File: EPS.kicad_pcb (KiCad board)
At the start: 4 copper layers, 90.2 x 95.9 mm, 6 parts

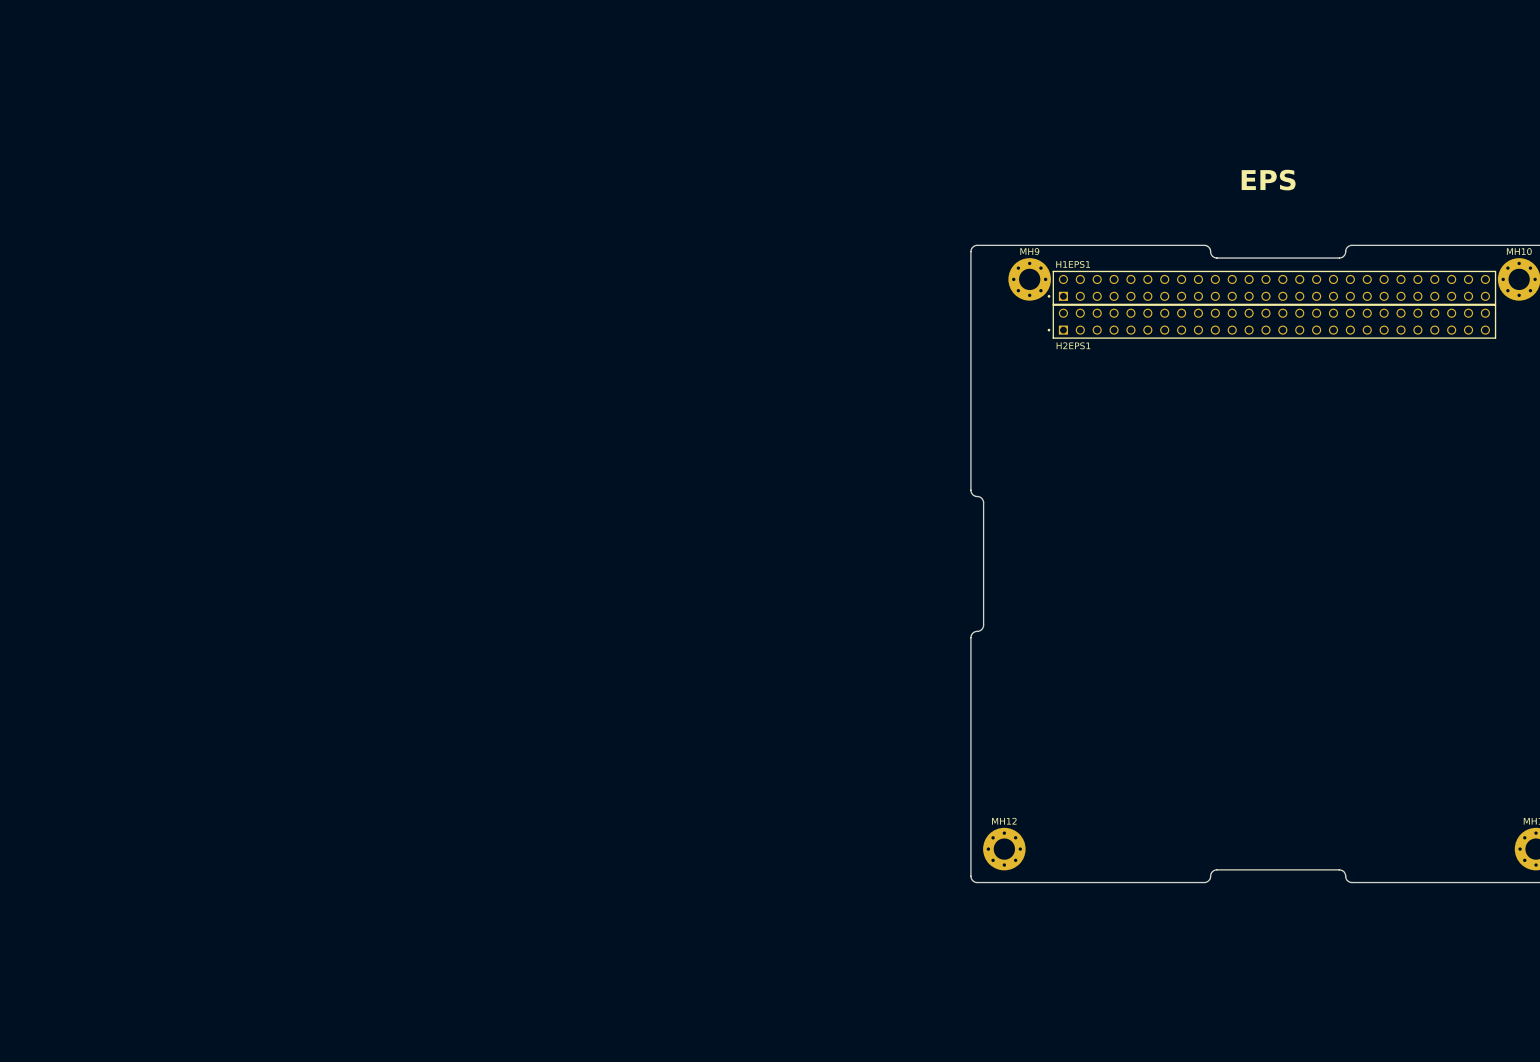
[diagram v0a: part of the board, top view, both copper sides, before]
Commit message: updated the schematic to remove connection to rocksat, linked schmatic symbols to footprints
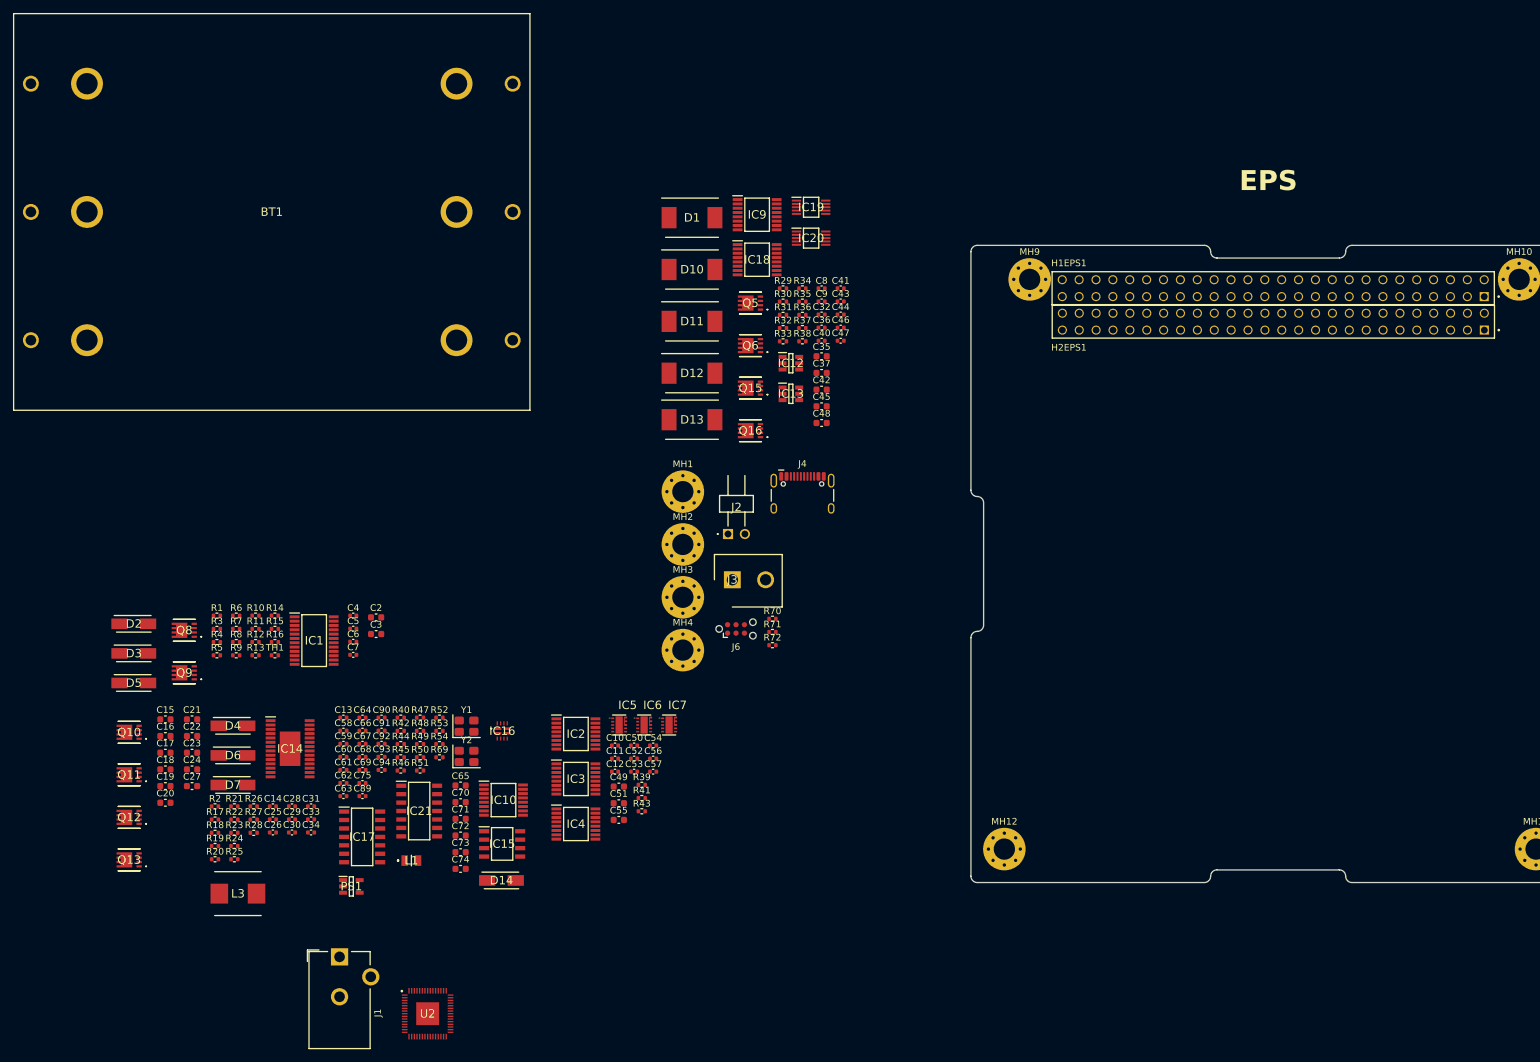
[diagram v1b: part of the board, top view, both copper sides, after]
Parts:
- added BT1: BK-18650-PC6, HEDGE2:BK18650PC6, F.Cu at (71.2, 86.3)
- added C10: 100n, Capacitor_SMD:C_0402_1005Metric, F.Cu at (122.8, 166.6)
- added C11: 100n, Capacitor_SMD:C_0402_1005Metric, F.Cu at (122.8, 168.6)
- added C12: 100n, Capacitor_SMD:C_0402_1005Metric, F.Cu at (122.8, 170.5)
- added C13: 100n, Capacitor_SMD:C_0402_1005Metric, F.Cu at (81.9, 162.4)
- added C14: 100n, Capacitor_SMD:C_0402_1005Metric, F.Cu at (71.3, 175.7)
- added C15: 33u, Capacitor_SMD:C_0603_1608Metric, F.Cu at (55.1, 162.7)
- added C16: 33u, Capacitor_SMD:C_0603_1608Metric, F.Cu at (55.1, 165.2)
- added C17: 33u, Capacitor_SMD:C_0603_1608Metric, F.Cu at (55.1, 167.7)
- added C18: 10u, Capacitor_SMD:C_0603_1608Metric, F.Cu at (55.1, 170.2)
- added C19: 10u, Capacitor_SMD:C_0603_1608Metric, F.Cu at (55.1, 172.7)
- added C2: 1u, Capacitor_SMD:C_0603_1608Metric, F.Cu at (86.8, 147.3)
- added C20: 22u, Capacitor_SMD:C_0603_1608Metric, F.Cu at (55.1, 175.2)
- added C21: 22u, Capacitor_SMD:C_0603_1608Metric, F.Cu at (59.1, 162.7)
- added C22: 22u, Capacitor_SMD:C_0603_1608Metric, F.Cu at (59.1, 165.2)
- added C23: 220u, Capacitor_SMD:C_0603_1608Metric, F.Cu at (59.1, 167.7)
- added C24: 220u, Capacitor_SMD:C_0603_1608Metric, F.Cu at (59.1, 170.2)
- added C25: 100n, Capacitor_SMD:C_0402_1005Metric, F.Cu at (71.3, 177.7)
- added C26: 100n, Capacitor_SMD:C_0402_1005Metric, F.Cu at (71.3, 179.7)
- added C27: 1u, Capacitor_SMD:C_0603_1608Metric, F.Cu at (59.1, 172.7)
- added C28: 100n, Capacitor_SMD:C_0402_1005Metric, F.Cu at (74.2, 175.7)
- added C29: 47p, Capacitor_SMD:C_0402_1005Metric, F.Cu at (74.2, 177.7)
- added C3: 1u, Capacitor_SMD:C_0603_1608Metric, F.Cu at (86.8, 149.8)
- added C30: 15n, Capacitor_SMD:C_0402_1005Metric, F.Cu at (74.2, 179.7)
- added C31: 15n, Capacitor_SMD:C_0402_1005Metric, F.Cu at (77.1, 175.7)
- added C32: 22n, Capacitor_SMD:C_0402_1005Metric, F.Cu at (153.9, 101.7)
- added C33: 180p, Capacitor_SMD:C_0402_1005Metric, F.Cu at (77.1, 177.7)
- added C34: 100p, Capacitor_SMD:C_0402_1005Metric, F.Cu at (77.1, 179.7)
- added C35: 47u, Capacitor_SMD:C_0603_1608Metric, F.Cu at (153.9, 108.0)
- added C36: 100n, Capacitor_SMD:C_0402_1005Metric, F.Cu at (153.9, 103.7)
- added C37: 22u, Capacitor_SMD:C_0603_1608Metric, F.Cu at (153.9, 110.5)
- added C4: 100n, Capacitor_SMD:C_0402_1005Metric, F.Cu at (83.4, 147.0)
- added C40: 22n, Capacitor_SMD:C_0402_1005Metric, F.Cu at (153.9, 105.7)
- added C41: 100n, Capacitor_SMD:C_0402_1005Metric, F.Cu at (156.8, 97.8)
- added C42: 22u, Capacitor_SMD:C_0603_1608Metric, F.Cu at (153.9, 113.0)
- added C43: 100n, Capacitor_SMD:C_0402_1005Metric, F.Cu at (156.8, 99.8)
- added C44: 100n, Capacitor_SMD:C_0402_1005Metric, F.Cu at (156.8, 101.7)
- added C45: 22u, Capacitor_SMD:C_0603_1608Metric, F.Cu at (153.9, 115.5)
- added C46: 100n, Capacitor_SMD:C_0402_1005Metric, F.Cu at (156.8, 103.7)
- added C47: 100n, Capacitor_SMD:C_0402_1005Metric, F.Cu at (156.8, 105.7)
- added C48: 22u, Capacitor_SMD:C_0603_1608Metric, F.Cu at (153.9, 118.1)
- added C49: 1u, Capacitor_SMD:C_0603_1608Metric, F.Cu at (123.4, 172.8)
- added C5: 100n, Capacitor_SMD:C_0402_1005Metric, F.Cu at (83.4, 149.0)
- added C50: 100n, Capacitor_SMD:C_0402_1005Metric, F.Cu at (125.7, 166.6)
- added C51: 1u, Capacitor_SMD:C_0603_1608Metric, F.Cu at (123.4, 175.3)
- added C52: 220p, Capacitor_SMD:C_0402_1005Metric, F.Cu at (125.7, 168.6)
- added C53: 220p, Capacitor_SMD:C_0402_1005Metric, F.Cu at (125.7, 170.5)
- added C54: 100n, Capacitor_SMD:C_0402_1005Metric, F.Cu at (128.5, 166.6)
- added C55: 1u, Capacitor_SMD:C_0603_1608Metric, F.Cu at (123.4, 177.8)
- added C56: 220p, Capacitor_SMD:C_0402_1005Metric, F.Cu at (128.5, 168.6)
- added C57: 100n, Capacitor_SMD:C_0402_1005Metric, F.Cu at (128.5, 170.5)
- added C58: 100n, Capacitor_SMD:C_0402_1005Metric, F.Cu at (81.9, 164.4)
- added C59: 100n, Capacitor_SMD:C_0402_1005Metric, F.Cu at (81.9, 166.3)
- added C6: 100n, Capacitor_SMD:C_0402_1005Metric, F.Cu at (83.4, 151.0)
- added C60: 100n, Capacitor_SMD:C_0402_1005Metric, F.Cu at (81.9, 168.3)
- added C61: 100n, Capacitor_SMD:C_0402_1005Metric, F.Cu at (81.9, 170.3)
- added C62: 100n, Capacitor_SMD:C_0402_1005Metric, F.Cu at (81.9, 172.2)
- added C63: 100n, Capacitor_SMD:C_0402_1005Metric, F.Cu at (81.9, 174.2)
- added C64: 100n, Capacitor_SMD:C_0402_1005Metric, F.Cu at (84.8, 162.4)
- added C65: 4u7, Capacitor_SMD:C_0603_1608Metric, F.Cu at (99.6, 172.6)
- added C66: 100n, Capacitor_SMD:C_0402_1005Metric, F.Cu at (84.8, 164.4)
- added C67: 100n, Capacitor_SMD:C_0402_1005Metric, F.Cu at (84.8, 166.3)
- added C68: 15p, Capacitor_SMD:C_0402_1005Metric, F.Cu at (84.8, 168.3)
- added C69: 15p, Capacitor_SMD:C_0402_1005Metric, F.Cu at (84.8, 170.3)
- added C7: 100n, Capacitor_SMD:C_0402_1005Metric, F.Cu at (83.4, 152.9)
- added C70: 4u7, Capacitor_SMD:C_0603_1608Metric, F.Cu at (99.6, 175.1)
- added C71: 4u7, Capacitor_SMD:C_0603_1608Metric, F.Cu at (99.6, 177.6)
- added C72: 4u7, Capacitor_SMD:C_0603_1608Metric, F.Cu at (99.6, 180.1)
- added C73: 1u, Capacitor_SMD:C_0603_1608Metric, F.Cu at (99.6, 182.7)
- added C74: 1u, Capacitor_SMD:C_0603_1608Metric, F.Cu at (99.6, 185.2)
- added C75: 100n, Capacitor_SMD:C_0402_1005Metric, F.Cu at (84.8, 172.2)
- added C8: 100n, Capacitor_SMD:C_0402_1005Metric, F.Cu at (153.9, 97.8)
- added C89: 100n, Capacitor_SMD:C_0402_1005Metric, F.Cu at (84.8, 174.2)
- added C9: 100n, Capacitor_SMD:C_0402_1005Metric, F.Cu at (153.9, 99.8)
- added C90: 100n, Capacitor_SMD:C_0402_1005Metric, F.Cu at (87.7, 162.4)
- added C91: 100n, Capacitor_SMD:C_0402_1005Metric, F.Cu at (87.7, 164.4)
- added C92: 100n, Capacitor_SMD:C_0402_1005Metric, F.Cu at (87.7, 166.3)
- added C93: 15p, Capacitor_SMD:C_0402_1005Metric, F.Cu at (87.7, 168.3)
- added C94: 15p, Capacitor_SMD:C_0402_1005Metric, F.Cu at (87.7, 170.3)
- added D1: SMCJ36A, HEDGE2:SMCJ36A, F.Cu at (134.4, 87.2)
- added D10: SMCJ36A, HEDGE2:SMCJ36A, F.Cu at (134.4, 95.0)
- added D11: SMCJ36A, HEDGE2:SMCJ36A, F.Cu at (134.4, 102.8)
- added D12: SMCJ36A, HEDGE2:SMCJ36A, F.Cu at (134.4, 110.6)
- added D13: SMCJ36A, HEDGE2:SMCJ36A, F.Cu at (134.4, 117.6)
- added D14: CDBA240LL-HF, 40V 2A, HEDGE2:CDBA240LL-HF, F.Cu at (105.7, 186.9)
- added D2: CDBA240LL-HF, 40V 2A, HEDGE2:CDBA240LL-HF, F.Cu at (50.4, 148.3)
- added D3: CDBA240LL-HF, 40V 2A, HEDGE2:CDBA240LL-HF, F.Cu at (50.4, 152.7)
- added D4: 40V 2A, HEDGE2:CDBA240LL-HF, F.Cu at (65.3, 163.6)
- added D5: CDBA240LL-HF, 40V 2A, HEDGE2:CDBA240LL-HF, F.Cu at (50.4, 157.2)
- added D6: CDBA240LL-HF, 40V 2A, HEDGE2:CDBA240LL-HF, F.Cu at (65.3, 168.1)
- added D7: 40V 2A, HEDGE2:CDBA240LL-HF, F.Cu at (65.3, 172.5)
- added IC1: BQ7791514PWR, HEDGE2:BQ7791501PWR, F.Cu at (77.5, 150.8)
- added IC10: INA260AIPWR, HEDGE2:INA260AIPWR, F.Cu at (106.0, 174.8)
- added IC12: LM74700QDBVRQ1, HEDGE2:LM74700QDBVRQ1, F.Cu at (149.3, 109.1)
- added IC13: LM74700QDBVRQ1, HEDGE2:LM74700QDBVRQ1, F.Cu at (149.3, 113.7)
- added IC14: LM5176PWPR, HEDGE2:LM5176PWPR, F.Cu at (73.9, 167.1)
- added IC15: SN65HVD1782QDRQ1, HEDGE2:SN65HVD1782QDRQ1, F.Cu at (105.8, 181.4)
- added IC16: TPS2121RUXR, HEDGE2:TPS2121RUXR, F.Cu at (105.8, 164.4)
- added IC17: TCAN1046AVDRQ1, HEDGE2:TCAN1046AVDRQ1, F.Cu at (84.7, 180.3)
- added IC18: INA260AIPWR, HEDGE2:INA260AIPWR, F.Cu at (144.2, 93.5)
- added IC19: LM5060Q1MM_NOPB, HEDGE2:LM5060Q1MM_NOPB, F.Cu at (152.3, 85.6)
- added IC2: INA260AIPWR, HEDGE2:INA260AIPWR, F.Cu at (116.9, 164.9)
- added IC20: LM5060Q1MM_NOPB, HEDGE2:LM5060Q1MM_NOPB, F.Cu at (152.3, 90.2)
- added IC21: MCP2517FD-H_SL, HEDGE2:MCP2517FD-H_SL, F.Cu at (93.3, 176.5)
- added IC3: INA260AIPWR, HEDGE2:INA260AIPWR, F.Cu at (116.9, 171.6)
- added IC4: INA260AIPWR, HEDGE2:INA260AIPWR, F.Cu at (116.9, 178.4)
- added IC5: TPS22990DMLR, HEDGE2:TPS22990DMLR, F.Cu at (123.4, 163.5)
- added IC6: TPS22990DMLR, HEDGE2:TPS22990DMLR, F.Cu at (127.2, 163.5)
- added IC7: TPS22990DMLR, HEDGE2:TPS22990DMLR, F.Cu at (130.9, 163.5)
- added IC9: INA260AIPWR, HEDGE2:INA260AIPWR, F.Cu at (144.2, 86.7)
- added J1: Barrel_Jack_Switch, Connector_BarrelJack:BarrelJack_CUI_PJ-102AH_Horizontal, F.Cu at (81.3, 198.4)
- added J2: PH1RA-02-UA, HEDGE2:PH1RA02UA, F.Cu at (139.8, 134.8)
- added J3: WJ126V-5.0-2P, HEDGE2:WJ126V-5.0-2P, F.Cu at (140.5, 141.7)
- added J4: USB_C_Receptacle_USB2.0_16P, Connector_USB:USB_C_Receptacle_HCTL_HC-TYPE-C-16P-01A, F.Cu at (151.0, 129.8)
- added J6: TagConnect_TC2030-NL, Connector:Tag-Connect_TC2030-IDC-NL_2x03_P1.27mm_Vertical, F.Cu at (141.0, 149.1)
- added L1: 3u3 AOTA-B201610S3R3-101-T, HEDGE2:AOTAB201610S3R3101T, F.Cu at (92.2, 183.9)
- added L3: 0630CDMCDDS-1R2MC, HEDGE2:0630CDMCDDS-1R2MC, F.Cu at (66.1, 188.9)
- added MH1: MountingHole_Pad, MountingHole:MountingHole_3.2mm_M3_Pad_Via, F.Cu at (133.0, 128.4)
- added MH2: MountingHole_Pad, MountingHole:MountingHole_3.2mm_M3_Pad_Via, F.Cu at (133.0, 136.3)
- added MH3: MountingHole_Pad, MountingHole:MountingHole_3.2mm_M3_Pad_Via, F.Cu at (133.0, 144.3)
- added MH4: MountingHole_Pad, MountingHole:MountingHole_3.2mm_M3_Pad_Via, F.Cu at (133.0, 152.2)
- added PS1: TLV75733PDBVR, HEDGE2:TLV75733PDBVR, F.Cu at (83.1, 187.8)
- added Q10: BSZ067N06LS3_G, HEDGE2:BSZ067N06LS3G, F.Cu at (49.7, 164.6)
- added Q11: BSZ067N06LS3_G, HEDGE2:BSZ067N06LS3G, F.Cu at (49.7, 171.0)
- added Q12: BSZ067N06LS3_G, HEDGE2:BSZ067N06LS3G, F.Cu at (49.7, 177.4)
- added Q13: BSZ067N06LS3_G, HEDGE2:BSZ067N06LS3G, F.Cu at (49.7, 183.8)
- added Q15: BSZ067N06LS3_G, HEDGE2:BSZ067N06LS3G, F.Cu at (143.2, 112.8)
- added Q16: BSZ067N06LS3_G, HEDGE2:BSZ067N06LS3G, F.Cu at (143.2, 119.2)
- added Q5: BSZ067N06LS3_G, HEDGE2:BSZ067N06LS3G, F.Cu at (143.2, 100.0)
- added Q6: BSZ067N06LS3_G, HEDGE2:BSZ067N06LS3G, F.Cu at (143.2, 106.4)
- added Q8: BSZ067N06LS3_G, HEDGE2:BSZ067N06LS3G, F.Cu at (58.0, 149.3)
- added Q9: BSZ067N06LS3_G, HEDGE2:BSZ067N06LS3G, F.Cu at (58.0, 155.7)
- added R1: 1k, Resistor_SMD:R_0402_1005Metric, F.Cu at (62.9, 147.1)
- added R10: 1M, Resistor_SMD:R_0402_1005Metric, F.Cu at (68.7, 147.1)
- added R11: 1M, Resistor_SMD:R_0402_1005Metric, F.Cu at (68.7, 149.0)
- added R12: 3M3, Resistor_SMD:R_0402_1005Metric, F.Cu at (68.7, 151.0)
- added R13: 450k, Resistor_SMD:R_0402_1005Metric, F.Cu at (68.7, 153.0)
- added R14: 100k, Resistor_SMD:R_0402_1005Metric, F.Cu at (71.6, 147.1)
- added R15: 10k, Resistor_SMD:R_0402_1005Metric, F.Cu at (71.6, 149.0)
- added R16: 10k, Resistor_SMD:R_0402_1005Metric, F.Cu at (71.6, 151.0)
- added R17: 10, Resistor_SMD:R_0402_1005Metric, F.Cu at (62.6, 177.7)
- added R18: 249k, Resistor_SMD:R_0402_1005Metric, F.Cu at (62.6, 179.7)
- added R19: 71k5, Resistor_SMD:R_0402_1005Metric, F.Cu at (62.6, 181.7)
- added R2: 9m, Resistor_SMD:R_0402_1005Metric, F.Cu at (62.6, 175.8)
- added R20: 2k, Resistor_SMD:R_0402_1005Metric, F.Cu at (62.6, 183.7)
- added R21: 105k, Resistor_SMD:R_0402_1005Metric, F.Cu at (65.5, 175.8)
- added R22: 20k, Resistor_SMD:R_0402_1005Metric, F.Cu at (65.5, 177.7)
- added R23: 10k, Resistor_SMD:R_0402_1005Metric, F.Cu at (65.5, 179.7)
- added R24: 100, Resistor_SMD:R_0402_1005Metric, F.Cu at (65.5, 181.7)
- added R25: 100, Resistor_SMD:R_0402_1005Metric, F.Cu at (65.5, 183.7)
- added R26: 93k1, Resistor_SMD:R_0402_1005Metric, F.Cu at (68.4, 175.8)
- added R27: 23k2, Resistor_SMD:R_0402_1005Metric, F.Cu at (68.4, 177.7)
- added R28: 7k5, Resistor_SMD:R_0402_1005Metric, F.Cu at (68.4, 179.7)
- added R29: 9k09, Resistor_SMD:R_0402_1005Metric, F.Cu at (148.1, 97.8)
- added R3: 1k, Resistor_SMD:R_0402_1005Metric, F.Cu at (62.9, 149.0)
- added R30: 100k, Resistor_SMD:R_0402_1005Metric, F.Cu at (148.1, 99.8)
- added R31: 200k, Resistor_SMD:R_0402_1005Metric, F.Cu at (148.1, 101.8)
- added R32: 38k3, Resistor_SMD:R_0402_1005Metric, F.Cu at (148.1, 103.8)
- added R33: 14k, Resistor_SMD:R_0402_1005Metric, F.Cu at (148.1, 105.8)
- added R34: 200k, Resistor_SMD:R_0402_1005Metric, F.Cu at (151.0, 97.8)
- added R35: 38k3, Resistor_SMD:R_0402_1005Metric, F.Cu at (151.0, 99.8)
- added R36: 14k, Resistor_SMD:R_0402_1005Metric, F.Cu at (151.0, 101.8)
- added R37: 9k09, Resistor_SMD:R_0402_1005Metric, F.Cu at (151.0, 103.8)
- added R38: 100k, Resistor_SMD:R_0402_1005Metric, F.Cu at (151.0, 105.8)
- added R39: 10k, Resistor_SMD:R_0402_1005Metric, F.Cu at (126.8, 172.5)
- added R4: 1k, Resistor_SMD:R_0402_1005Metric, F.Cu at (62.9, 151.0)
- added R40: 27, Resistor_SMD:R_0402_1005Metric, F.Cu at (90.6, 162.4)
- added R41: 10k, Resistor_SMD:R_0402_1005Metric, F.Cu at (126.8, 174.5)
- added R42: 27, Resistor_SMD:R_0402_1005Metric, F.Cu at (90.6, 164.4)
- added R43: 10k, Resistor_SMD:R_0402_1005Metric, F.Cu at (126.8, 176.5)
- added R44: 1k, Resistor_SMD:R_0402_1005Metric, F.Cu at (90.6, 166.4)
- added R45: 33, Resistor_SMD:R_0402_1005Metric, F.Cu at (90.6, 168.4)
- added R46: 23k7, Resistor_SMD:R_0402_1005Metric, F.Cu at (90.6, 170.4)
- added R47: 5k, Resistor_SMD:R_0402_1005Metric, F.Cu at (93.5, 162.4)
- added R48: 23k7, Resistor_SMD:R_0402_1005Metric, F.Cu at (93.5, 164.4)
- added R49: 5k, Resistor_SMD:R_0402_1005Metric, F.Cu at (93.5, 166.4)
- added R5: 1k, Resistor_SMD:R_0402_1005Metric, F.Cu at (62.9, 153.0)
- added R50: 51k1, Resistor_SMD:R_0402_1005Metric, F.Cu at (93.5, 168.4)
- added R51: 4k7, Resistor_SMD:R_0402_1005Metric, F.Cu at (93.5, 170.4)
- added R52: 4k7, Resistor_SMD:R_0402_1005Metric, F.Cu at (96.4, 162.4)
- added R53: 10k, Resistor_SMD:R_0402_1005Metric, F.Cu at (96.4, 164.4)
- added R54: 60, Resistor_SMD:R_0402_1005Metric, F.Cu at (96.4, 166.4)
- added R6: 1k, Resistor_SMD:R_0402_1005Metric, F.Cu at (65.8, 147.1)
- added R69: 60, Resistor_SMD:R_0402_1005Metric, F.Cu at (96.4, 168.4)
- added R7: 10m, Resistor_SMD:R_0402_1005Metric, F.Cu at (65.8, 149.0)
- added R70: 5k1, Resistor_SMD:R_0402_1005Metric, F.Cu at (146.5, 147.5)
- added R71: 5k1, Resistor_SMD:R_0402_1005Metric, F.Cu at (146.5, 149.5)
- added R72: 4k7, Resistor_SMD:R_0402_1005Metric, F.Cu at (146.5, 151.5)
- added R8: 4k5, Resistor_SMD:R_0402_1005Metric, F.Cu at (65.8, 151.0)
- added R9: 1M, Resistor_SMD:R_0402_1005Metric, F.Cu at (65.8, 153.0)
- added TH1: 10k, Resistor_SMD:R_0402_1005Metric, F.Cu at (71.6, 153.0)
- added U2: RP2354A_60QFN, HEDGE2:RP2354A, F.Cu at (94.6, 206.9)
- added Y1: ABM8AIG-20MHz-12-2Z-T3, Crystal:Crystal_SMD_3225-4Pin_3.2x2.5mm, F.Cu at (100.5, 163.7)
- added Y2: ABM8-272-T3, Crystal:Crystal_SMD_3225-4Pin_3.2x2.5mm, F.Cu at (100.5, 168.2)
- H1EPS1, H2EPS1: footprint ESQ-126-39-G-D:SAMTEC_ESQ-126-39-G-D -> HEDGE2:SAMTEC_ESQ-126-39-G-D
- moved H2EPS1 63.3 mm to (253.6, 104.1)
- moved H1EPS1 63.3 mm to (253.6, 99.0)
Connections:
- net /EPS/5V_PERM renamed /5V_PERM
- net /EPS/BATT renamed /BATT
- net /EPS/CAN_A_H renamed /CAN_A_H
- net /EPS/CAN_A_L renamed /CAN_A_L
- net /EPS/CAN_B_H renamed /CAN_B_H
- net /EPS/CAN_B_L renamed /CAN_B_L
- net /EPS/CHARGE renamed /CHARGE
- net /EPS/DS_A renamed /DS_A
- net /EPS/DS_B renamed /DS_B
- net /EPS/DS_C renamed /DS_C
- net /EPS/ENA_PWR_1 renamed /ENA_PWR_1
- net /EPS/ENA_PWR_2 renamed /ENA_PWR_2
- net /EPS/ENA_PWR_3 renamed /ENA_PWR_3
- net /EPS/ENA_PWR_4 renamed /ENA_PWR_4
- net /EPS/ENA_PWR_5 renamed /ENA_PWR_5
- net /EPS/ENA_PWR_6 renamed /ENA_PWR_6
- net /EPS/ENA_PWR_7 renamed /ENA_PWR_7
- net /EPS/ENA_PWR_8 renamed /ENA_PWR_8
- net /EPS/PWR_1 renamed /PWR_1
- net /EPS/PWR_2 renamed /PWR_2
- net /EPS/PWR_3 renamed /PWR_3
- net /EPS/PWR_4 renamed /PWR_4
- net /EPS/PWR_5 renamed /PWR_5
- net /EPS/PWR_6 renamed /PWR_6
- net /EPS/PWR_7 renamed /PWR_7
- net /EPS/PWR_8 renamed /PWR_8
- net /EPS/RBF_A renamed /RBF_A
- net /EPS/RBF_B renamed /RBF_B
- net /EPS/RBF_C renamed /RBF_C
- net /EPS/UART_A_RX renamed /UART_A_RX
- net /EPS/UART_A_TX renamed /UART_A_TX
- net /EPS/UART_B_RX renamed /UART_B_RX
- net /EPS/UART_B_TX renamed /UART_B_TX
- net /EPS/UART_C_RX renamed /UART_C_RX
- net /EPS/UART_C_TX renamed /UART_C_TX
- net /EPS/UART_D_RX renamed /UART_D_RX
- net /EPS/UART_D_TX renamed /UART_D_TX
- net /EPS/UART_E_RX renamed /UART_E_RX
- net /EPS/UART_E_TX renamed /UART_E_TX
- net /EPS/UART_F_RX renamed /UART_F_RX
- net /EPS/UART_F_TX renamed /UART_F_TX
- H1EPS1 pad 29: GND -> +BATT
- H1EPS1 pad 30: GND -> +BATT
- H1EPS1 pad 31: GND -> +BATT
- H1EPS1 pad 32: GND -> +BATT
- H2EPS1 pad 29: GND -> +BATT
- H2EPS1 pad 30: GND -> +BATT
- H2EPS1 pad 31: GND -> +BATT
- H2EPS1 pad 32: GND -> +BATT

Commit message: began initial layout
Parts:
- removed the MH1 at (133.0, 128.4)
- removed the MH2 at (133.0, 136.3)
- removed the MH3 at (133.0, 144.3)
- removed the MH4 at (133.0, 152.2)
- moved U2 143.9 mm to (217.8, 132.5)
- moved J6 119.5 mm to (260.2, 158.2), turned to -90 degrees
- moved J3 117.4 mm to (257.8, 140.0), turned to 90 degrees
- moved J2 114.3 mm to (253.4, 147.4), turned to -90 degrees
- moved R70 108.6 mm to (252.1, 122.0)
- moved R71 108.4 mm to (252.1, 125.2)
- moved J4 107.7 mm to (258.6, 123.9), turned to 90 degrees
- moved R72 104.5 mm to (250.9, 146.5), turned to 90 degrees
- moved C55 97.4 mm to (220.8, 180.3)
- moved C50 96.2 mm to (221.5, 158.9)
- moved IC5 95.9 mm to (219.2, 159.8)
- moved R39 95.6 mm to (221.7, 160.1)
- moved C14 95.3 mm to (165.1, 192.5)
- moved C25 95.3 mm to (165.1, 194.4)
- moved C26 95.3 mm to (165.1, 196.4)
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- renumbered MH9 to MH1, MH10 to MH2, MH12 to MH3, MH11 to MH4

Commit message: Added most 3d models, continued layout
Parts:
- added MH2: MountingHole_Pad, MountingHole:MountingHole_3.2mm_M3_Pad_Via, F.Cu at (259.1, 96.4)
- BT1, C2, C3, C4, C5, C6, C7, D2, D3, D5, IC1, J1, Q8, Q9, R1, R10, R11, R12, R13, R14, R15, R16, R3, R4, R5, R6, R7, R8, R9, TH1: moved to B.Cu
- moved J1 171.0 mm to (245.5, 172.7), turned to 180 degrees
- moved BT1 158.5 mm to (218.6, 137.7)
- moved D3 147.2 mm to (233.5, 179.1), turned to 180 degrees
- moved D5 147.2 mm to (233.5, 183.5), turned to 180 degrees
- moved C90 146.9 mm to (282.3, 182.6), turned to 90 degrees
- moved C89 144.8 mm to (282.9, 178.5), turned to 180 degrees
- moved IC17 139.6 mm to (277.9, 182.8)
- moved C91 137.9 mm to (273.1, 183.3), turned to -90 degrees
- moved R54 136.8 mm to (282.9, 179.7)
- moved R69 136.5 mm to (282.9, 180.9), turned to 180 degrees
- moved Q8 132.4 mm to (225.9, 175.6), turned to 180 degrees
- moved Q9 132.4 mm to (225.9, 182.0), turned to 180 degrees
- moved R1 122.8 mm to (221.0, 173.4), turned to 180 degrees
- moved R3 122.8 mm to (221.0, 175.4), turned to 180 degrees
- moved R4 122.8 mm to (221.0, 177.4), turned to 180 degrees
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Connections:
- C6 pad 1: unconnected-(C6-Pad1) -> Net-(IC1-VC1)
- MH1 pad 1: GND -> +BATT
- MH3 pad 1: GND -> +BATT
- MH4 pad 1: GND -> +BATT
- U2 pad 23: unconnected-(U2-DVDD-Pad23) -> +BATT
- U2 pad 6: unconnected-(U2-DVDD-Pad6) -> +BATT
- Y1 pad 2: unconnected-(Y1-Pad2) -> +BATT

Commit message: Initial layout completed
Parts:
- removed the MH2 at (258.9, 96.5)
- added C1: 100n, Capacitor_SMD:C_0402_1005Metric, F.Cu at (208.0, 137.4)
- D4, D7: value 40V 2A -> CDBA240LL-HF, 40V 2A
- moved D13 128.7 mm to (252.4, 168.9), turned to 90 degrees
- moved Q6 128.5 mm to (246.6, 182.6), turned to 90 degrees
- moved D12 125.6 mm to (245.6, 168.9), turned to 90 degrees
- moved D11 122.5 mm to (235.1, 172.6), turned to 90 degrees
- moved C41 121.4 mm to (248.2, 177.6), turned to 90 degrees
- moved Q5 118.4 mm to (229.4, 181.2), turned to 90 degrees
- moved D10 117.3 mm to (225.2, 169.3)
- moved IC13 115.7 mm to (245.8, 177.6), turned to -90 degrees
- moved IC9 115.3 mm to (253.0, 124.9), turned to 180 degrees
- moved C40 114.6 mm to (245.2, 174.9)
- moved Q13 108.0 mm to (235.8, 144.4), turned to 180 degrees
- moved C89 106.4 mm to (195.8, 117.4), turned to -90 degrees
- moved R54 106.1 mm to (197.0, 117.4), turned to 90 degrees
- moved R69 105.9 mm to (198.2, 117.4), turned to -90 degrees
- moved C36 105.6 mm to (230.8, 176.1), turned to 90 degrees
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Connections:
- BT1 pad 1+: +BATT -> /Batteries/VC1
- BT1 pad 1-: +BATT -> GND
- BT1 pad 2+: +BATT -> /Batteries/VC2
- BT1 pad 2-: +BATT -> /Batteries/VC1
- BT1 pad 3-: +BATT -> /Batteries/VC2
- C10 pad 2: +BATT -> GND
- C11 pad 2: +BATT -> GND
- C12 pad 2: +BATT -> GND
- C13 pad 2: +BATT -> GND
- C14 pad 2: +BATT -> GND
- C15 pad 2: +BATT -> GND
- C16 pad 2: +BATT -> GND
- C17 pad 2: +BATT -> GND
- C18 pad 2: +BATT -> GND
- C19 pad 2: +BATT -> GND
- C2 pad 2: +BATT -> GND
- C20 pad 2: +BATT -> GND
- C21 pad 2: +BATT -> GND
- C22 pad 2: +BATT -> GND
- C23 pad 2: +BATT -> GND
- C24 pad 2: +BATT -> GND
- C25 pad 2: +BATT -> GND
- C27 pad 2: +BATT -> GND
- C3 pad 1: +BATT -> GND
- C30 pad 2: +BATT -> GND
- C32 pad 2: +BATT -> GND
- C33 pad 2: +BATT -> GND
- C34 pad 2: +BATT -> GND
- C35 pad 2: +BATT -> GND
- C37 pad 2: +BATT -> GND
- C40 pad 2: +BATT -> GND
- C42 pad 2: +BATT -> GND
- C43 pad 2: +BATT -> GND
- C44 pad 2: +BATT -> GND
- C45 pad 2: +BATT -> GND
- C46 pad 2: +BATT -> GND
- C47 pad 2: +BATT -> GND
- C48 pad 2: +BATT -> GND
- C49 pad 2: +BATT -> GND
- C50 pad 2: +BATT -> GND
- C51 pad 2: +BATT -> GND
- C52 pad 2: +BATT -> GND
- C53 pad 2: +BATT -> GND
- C54 pad 2: +BATT -> GND
- C55 pad 2: +BATT -> GND
- C56 pad 2: +BATT -> GND
- C57 pad 2: +BATT -> GND
- C58 pad 2: +BATT -> GND
- C59 pad 2: +BATT -> GND
- C6 pad 2: +BATT -> GND
- C60 pad 2: +BATT -> GND
- C61 pad 2: +BATT -> GND
- C62 pad 2: +BATT -> GND
- C63 pad 2: +BATT -> GND
- C64 pad 2: +BATT -> GND
- C65 pad 2: +BATT -> GND
- C66 pad 2: +BATT -> GND
- C67 pad 2: +BATT -> GND
- C68 pad 1: +BATT -> GND
- C69 pad 1: +BATT -> GND
- C7 pad 1: +BATT -> GND
- C70 pad 2: +BATT -> GND
- C71 pad 2: +BATT -> GND
- C72 pad 2: +BATT -> GND
- C73 pad 2: +BATT -> GND
- C74 pad 2: +BATT -> GND
- C75 pad 2: +BATT -> GND
- C8 pad 2: +BATT -> GND
- C89 pad 2: +BATT -> GND
- C9 pad 2: +BATT -> GND
- C90 pad 2: +BATT -> GND
- C91 pad 2: +BATT -> GND
- C92 pad 2: +BATT -> GND
- C93 pad 1: +BATT -> GND
- C93 pad 2: Net-(IC21-OSC2) -> Net-(C93-Pad2)
- C94 pad 1: +BATT -> GND
- D1 pad 2: +BATT -> GND
- D11 pad 1: +BATT -> GND
- D13 pad 1: +BATT -> GND
- D14 pad 1: +BATT -> GND
- D3 pad 2: Net-(D3-A) -> PACK-
- H1EPS1 pad 29: +BATT -> GND
- H1EPS1 pad 30: +BATT -> GND
- H1EPS1 pad 31: +BATT -> GND
- H1EPS1 pad 32: +BATT -> GND
- H2EPS1 pad 29: +BATT -> GND
- H2EPS1 pad 30: +BATT -> GND
- H2EPS1 pad 31: +BATT -> GND
- H2EPS1 pad 32: +BATT -> GND
- IC1 pad 10: +BATT -> GND
- IC1 pad 20: +BATT -> GND
- IC1 pad 23: +BATT -> GND
- IC1 pad 24: +BATT -> GND
- IC1 pad 9: +BATT -> GND
- IC10 pad 11: +BATT -> GND
- IC10 pad 6: +BATT -> GND
- IC12 pad 2: +BATT -> GND
- IC13 pad 2: +BATT -> GND
- IC14 pad 10: +BATT -> GND
- IC14 pad 13: +BATT -> GND
- IC14 pad 14: +BATT -> GND
- IC14 pad 22: +BATT -> GND
- IC14 pad 29: +BATT -> GND
- IC14 pad 5: +BATT -> GND
- IC15 pad 5: +BATT -> GND
- IC16 pad 3: +BATT -> GND
- IC16 pad 6: +BATT -> GND
- IC16 pad 9: +BATT -> GND
- IC17 pad 14: +BATT -> GND
- IC17 pad 2: +BATT -> GND
- IC17 pad 5: +BATT -> GND
- IC18 pad 11: +BATT -> GND
- IC18 pad 4: +BATT -> GND
- IC18 pad 6: +BATT -> GND
- IC19 pad 6: +BATT -> GND
- IC2 pad 11: +BATT -> GND
- IC2 pad 4: +BATT -> GND
- IC2 pad 6: +BATT -> GND
- IC20 pad 6: +BATT -> GND
- IC21 pad 5: Net-(IC21-OSC2) -> unconnected-(IC21-OSC2-Pad5)
- IC21 pad 7: +BATT -> GND
- IC3 pad 11: +BATT -> GND
- IC3 pad 5: +BATT -> GND
- IC3 pad 6: +BATT -> GND
- IC4 pad 11: +BATT -> GND
- IC4 pad 6: +BATT -> GND
- IC5 pad 6: +BATT -> GND
- IC6 pad 6: +BATT -> GND
- IC7 pad 6: +BATT -> GND
- IC9 pad 11: +BATT -> GND
- IC9 pad 4: +BATT -> GND
- IC9 pad 6: +BATT -> GND
- J1 pad 2: +BATT -> PACK-
- J2 pad 2: +BATT -> GND
- J3 pad 2: +BATT -> GND
- J4 pad A1: +BATT -> GND
- J4 pad A12: +BATT -> GND
- J4 pad B1: +BATT -> GND
- J4 pad B12: +BATT -> GND
- J4 pad S1: +BATT -> GND
- J6 pad 5: +BATT -> GND
- MH1 pad 1: +BATT -> GND
- MH2 pad 1: +BATT -> GND
- MH3 pad 1: +BATT -> GND
- MH4 pad 1: +BATT -> GND
- PS1 pad 2: +BATT -> GND
- Q9 pad 1: Net-(D3-A) -> PACK-
- Q9 pad 2: Net-(D3-A) -> PACK-
- Q9 pad 3: Net-(D3-A) -> PACK-
- R12 pad 1: Net-(D3-A) -> PACK-
- R13 pad 1: Net-(D3-A) -> PACK-
- R14 pad 2: +BATT -> GND
- R16 pad 2: +BATT -> GND
- R19 pad 1: +BATT -> GND
- R2 pad 2: +BATT -> GND
- R22 pad 2: +BATT -> GND
- R25 pad 2: +BATT -> GND
- R26 pad 1: +BATT -> GND
- R27 pad 1: +BATT -> GND
- R28 pad 1: +BATT -> GND
- R33 pad 1: +BATT -> GND
- R36 pad 1: +BATT -> GND
- R4 pad 1: +BATT -> /Batteries/VC2
- R47 pad 2: +BATT -> GND
- R49 pad 2: +BATT -> GND
- R5 pad 1: +BATT -> /Batteries/VC1
- R50 pad 2: +BATT -> GND
- R6 pad 1: +BATT -> GND
- R7 pad 1: +BATT -> GND
- R70 pad 1: +BATT -> GND
- R71 pad 1: +BATT -> GND
- TH1 pad 2: +BATT -> GND
- U2 pad 1: +BATT -> 3V3
- U2 pad 11: +BATT -> 3V3
- U2 pad 20: +BATT -> 3V3
- U2 pad 23: +BATT -> 1V1
- U2 pad 30: +BATT -> 3V3
- U2 pad 38: +BATT -> 3V3
- U2 pad 39: +BATT -> 1V1
- U2 pad 44: +BATT -> 3V3
- U2 pad 45: +BATT -> 3V3
- U2 pad 47: +BATT -> GND
- U2 pad 53: +BATT -> 3V3
- U2 pad 54: +BATT -> 3V3
- U2 pad 6: +BATT -> 1V1
- U2 pad 61: +BATT -> GND
- Y1 pad 1: Net-(IC21-OSC2) -> Net-(C93-Pad2)
- Y1 pad 2: +BATT -> GND
- Y1 pad 4: +BATT -> GND
- Y2 pad 2: +BATT -> GND
- Y2 pad 4: +BATT -> GND
